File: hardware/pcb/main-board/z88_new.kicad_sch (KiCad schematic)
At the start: 0 parts

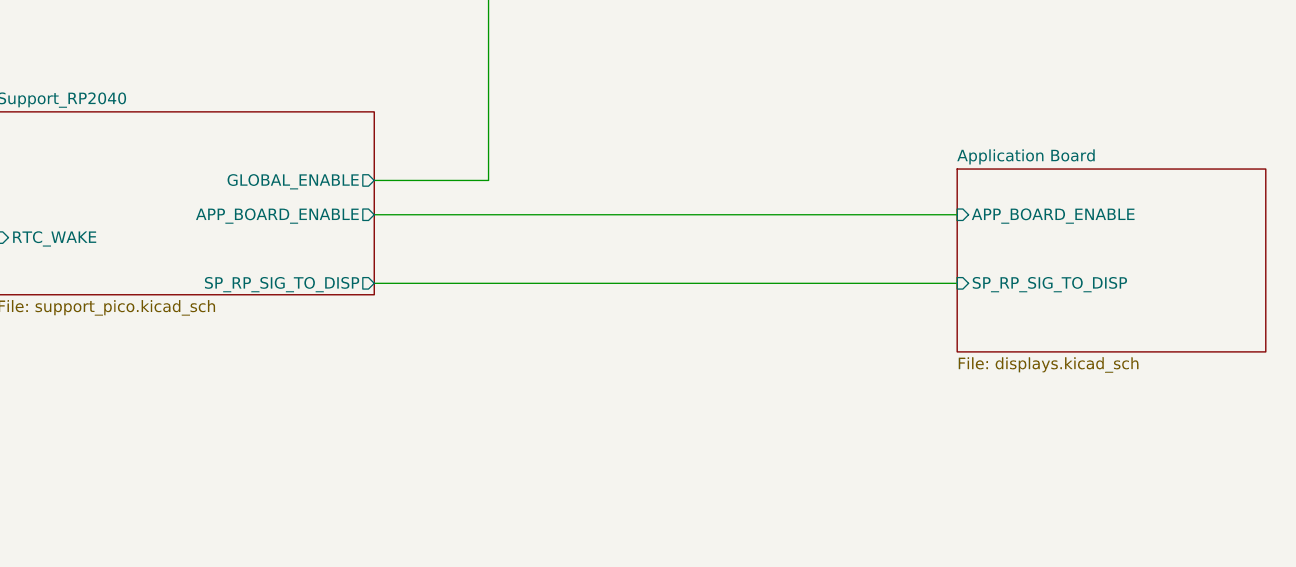
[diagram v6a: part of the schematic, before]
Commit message: more renaming and tidying up of internal interfaces
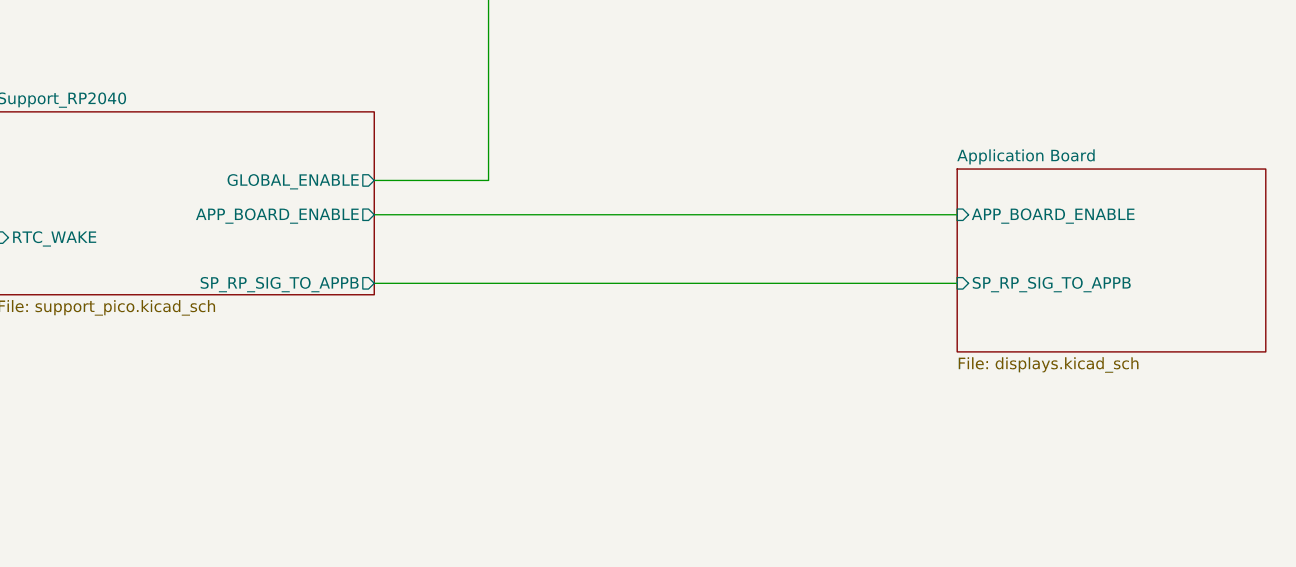
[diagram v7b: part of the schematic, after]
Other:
- sheet Application Board ports: added SP_RP_SIG_TO_APPB; removed SP_RP_SIG_TO_DISP
- sheet Support_RP2040 ports: added SP_RP_SIG_TO_APPB; removed SP_RP_SIG_TO_DISP
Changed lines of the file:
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@@
 			)
 		)
-		(pin "SP_RP_SIG_TO_DISP" output
+		(pin "SP_RP_SIG_TO_APPB" output
 			(at 162.56 148.59 0)
 			(effects
@@
 			)
 		)
-		(pin "SP_RP_SIG_TO_DISP" input
+		(pin "SP_RP_SIG_TO_APPB" input
 			(at 227.33 148.59 180)
 			(effects
